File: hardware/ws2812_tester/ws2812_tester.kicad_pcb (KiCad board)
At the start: 2 copper layers, 25 x 25 mm, 14 parts, among them J1 USB_C_DEALON-USB-US31-106, J2 Pins_1-4, J3 Conn_01x03, J4 Pins_5-8, U1 ATtiny85-20S

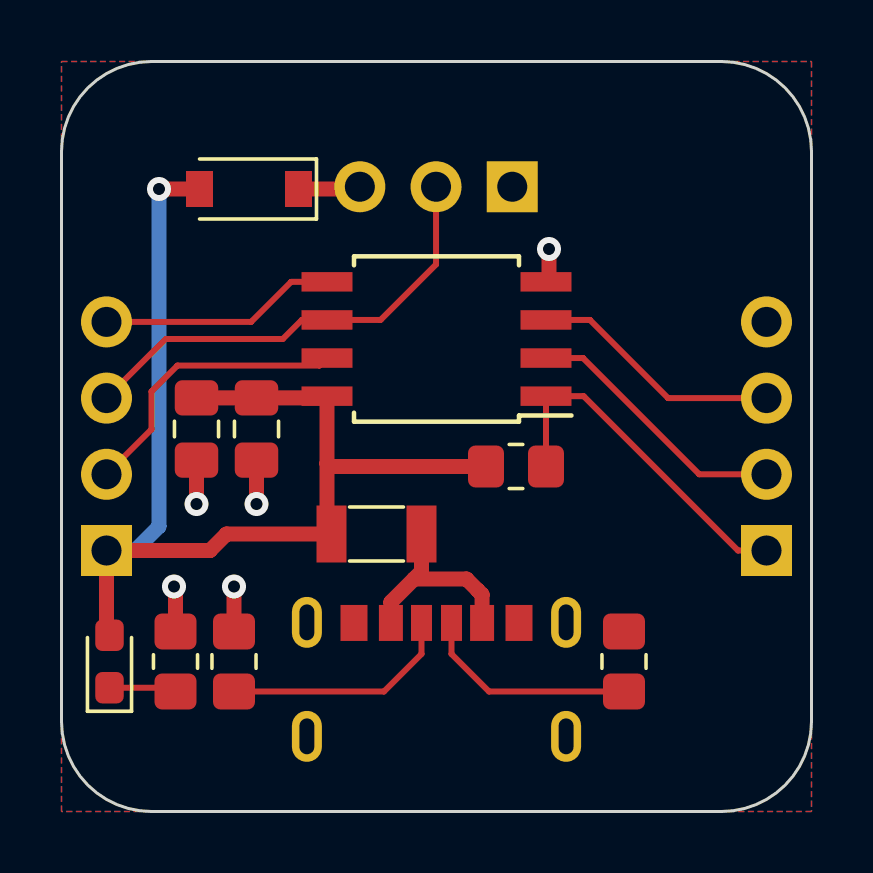
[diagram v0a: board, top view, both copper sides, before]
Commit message: Moves LED connector closer to the edge
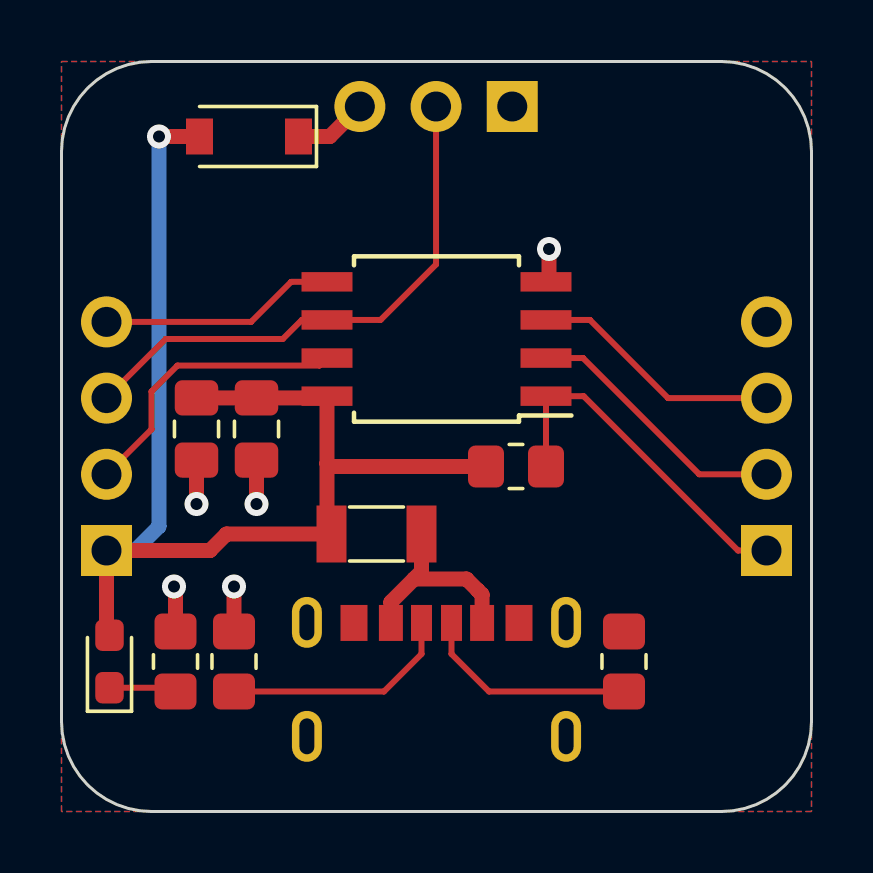
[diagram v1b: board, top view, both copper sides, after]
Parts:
- moved J3 2.67 mm to (153.0, 101.5)
- moved D2 1.75 mm to (144.2, 102.5)
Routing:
- net PB1/LED_DATA: track 15.4 -> 18.1 mm
- net VCC: track 39.6 -> 41.4 mm
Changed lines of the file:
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@@
   )
   (footprint "Diode_SMD:D_SOD-123" (layer "F.Cu")
-    (at 144.25 104.25 180)
+    (at 144.25 102.5 180)
     (descr "SOD-123")
     (tags "SOD-123")
@@
   )
   (footprint "Connector_PinHeader_2.54mm:PinHeader_1x03_P2.54mm_Horizontal" (layer "B.Cu")
-    (at 153.025 104.175 90)
+    (at 153.025 101.5 90)
     (descr "Through hole angled pin header, 1x03, 2.54mm pitch, 6mm pin length, single row")
     (tags "Through hole angled pin header THT 1x03 2.54mm single row")
@@
   (segment (start 152.15 113.5) (end 146.95 113.5) (width 0.5) (layer "F.Cu") (net 1))
   (segment (start 139.5 116.3) (end 142.95 116.3) (width 0.5) (layer "F.Cu") (net 1))
-  (segment (start 141.25 104.25) (end 142.6 104.25) (width 0.5) (layer "F.Cu") (net 1))
   (segment (start 146.85 111.155) (end 146.85 113.4) (width 0.5) (layer "F.Cu") (net 1))
   (segment (start 146.85 113.4) (end 146.85 115.6) (width 0.5) (layer "F.Cu") (net 1))
   (segment (start 142.95 116.3) (end 143.5 115.75) (width 0.5) (layer "F.Cu") (net 1))
+  (segment (start 141.25 102.5) (end 142.6 102.5) (width 0.5) (layer "F.Cu") (net 1))
   (segment (start 139.5 119.025) (end 139.6 119.125) (width 0.5) (layer "F.Cu") (net 1))
   (segment (start 146.95 113.5) (end 146.85 113.4) (width 0.5) (layer "F.Cu") (net 1))
@@
   (segment (start 143.5 115.75) (end 147 115.75) (width 0.5) (layer "F.Cu") (net 1))
   (segment (start 139.5 116.3) (end 139.5 119.025) (width 0.5) (layer "F.Cu") (net 1))
-  (via (at 141.25 104.25) (size 0.8) (drill 0.4) (layers "F.Cu" "B.Cu") (net 1))
-  (segment (start 141.25 115.5) (end 141.25 104.25) (width 0.5) (layer "B.Cu") (net 1))
-  (segment (start 139.5 116.3) (end 140.45 116.3) (width 0.5) (layer "B.Cu") (net 1))
-  (segment (start 140.45 116.3) (end 141.25 115.5) (width 0.5) (layer "B.Cu") (net 1))
+  (via (at 141.25 102.5) (size 0.8) (drill 0.4) (layers "F.Cu" "B.Cu") (net 1))
+  (segment (start 141.25 115.5) (end 140.45 116.3) (width 0.5) (layer "B.Cu") (net 1))
+  (segment (start 141.25 102.5) (end 141.25 115.5) (width 0.5) (layer "B.Cu") (net 1))
+  (segment (start 140.45 116.3) (end 139.5 116.3) (width 0.5) (layer "B.Cu") (net 1))
   (segment (start 154.25 106.25) (end 154.25 107.245) (width 0.5) (layer "F.Cu") (net 2))
   (segment (start 154.25 107.245) (end 154.15 107.345) (width 0.5) (layer "F.Cu") (net 2))
@@
   (via (at 143.75 117.5) (size 0.8) (drill 0.4) (layers "F.Cu" "B.Cu") (net 2))
   (via (at 142.5 114.75) (size 0.8) (drill 0.4) (layers "F.Cu" "B.Cu") (net 2))
-  (segment (start 147.87 104.25) (end 147.945 104.175) (width 0.5) (layer "F.Cu") (net 3))
-  (segment (start 145.9 104.25) (end 147.87 104.25) (width 0.5) (layer "F.Cu") (net 3))
+  (segment (start 145.9 102.5) (end 146.945 102.5) (width 0.5) (layer "F.Cu") (net 3))
+  (segment (start 146.945 102.5) (end 147.945 101.5) (width 0.5) (layer "F.Cu") (net 3))
   (segment (start 149.75 117.25) (end 151.5 117.25) (width 0.5) (layer "F.Cu") (net 4))
   (segment (start 152.02 117.77) (end 152.02 118.715) (width 0.5) (layer "F.Cu") (net 4))
@@
   (segment (start 158.22 111.22) (end 161.5 111.22) (width 0.2) (layer "F.Cu") (net 9))
   (segment (start 154.15 108.615) (end 155.615 108.615) (width 0.2) (layer "F.Cu") (net 9))
+  (segment (start 150.485 106.765) (end 150.485 101.5) (width 0.2) (layer "F.Cu") (net 10))
   (segment (start 146.01 108.615) (end 146.85 108.615) (width 0.2) (layer "F.Cu") (net 10))
   (segment (start 146.85 108.615) (end 148.635 108.615) (width 0.2) (layer "F.Cu") (net 10))
-  (segment (start 150.485 106.765) (end 150.485 104.175) (width 0.2) (layer "F.Cu") (net 10))
   (segment (start 141.47 109.25) (end 145.375 109.25) (width 0.2) (layer "F.Cu") (net 10))
   (segment (start 145.375 109.25) (end 146.01 108.615) (width 0.2) (layer "F.Cu") (net 10))
+  (segment (start 139.5 111.22) (end 141.47 109.25) (width 0.2) (layer "F.Cu") (net 10))
   (segment (start 148.635 108.615) (end 150.485 106.765) (width 0.2) (layer "F.Cu") (net 10))
-  (segment (start 139.5 111.22) (end 141.47 109.25) (width 0.2) (layer "F.Cu") (net 10))
   (segment (start 141 111) (end 141 112.26) (width 0.2) (layer "F.Cu") (net 11))
   (segment (start 141 112.26) (end 139.5 113.76) (width 0.2) (layer "F.Cu") (net 11))

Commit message: Adds labels for the Pins
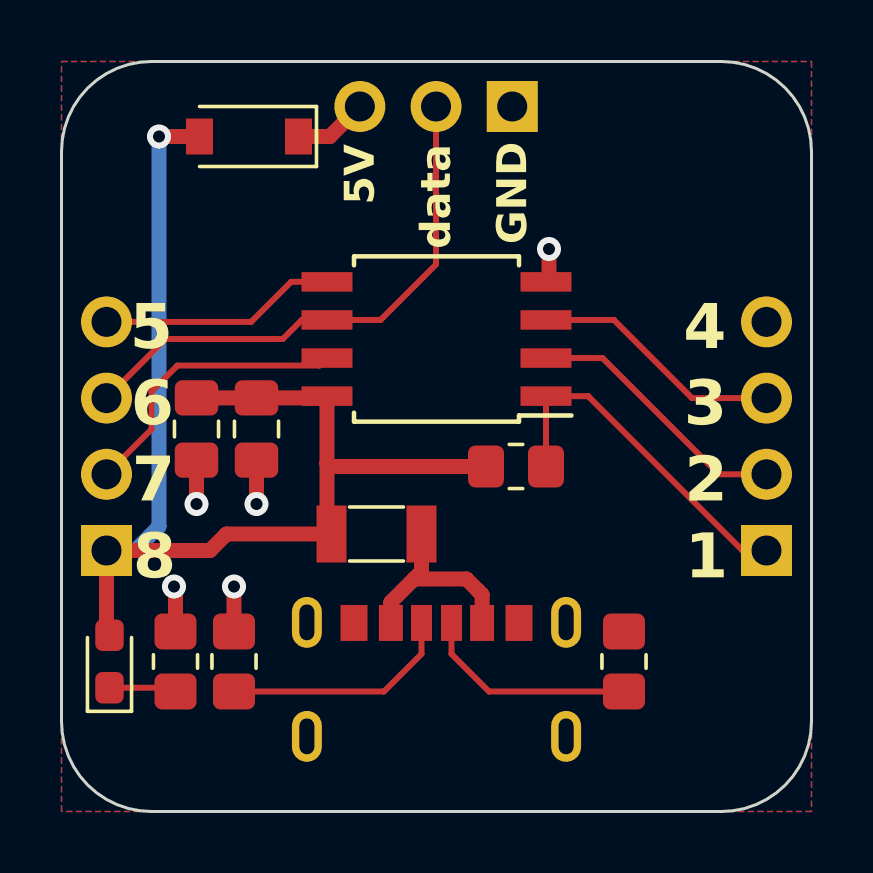
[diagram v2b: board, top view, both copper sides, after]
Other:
- board text added: "1"
- board text added: "2"
- board text added: "3"
- board text added: "4"
- board text added: "5"
- board text added: "5V"
- board text added: "6"
- board text added: "7"
- board text added: "8"
- board text added: "GND"
- board text added: "data"
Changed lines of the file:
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@@
   (gr_arc (start 138 103) (mid 138.87868 100.87868) (end 141 100)
     (stroke (width 0.1) (type default)) (layer "Edge.Cuts"))
+  (gr_text "6" (at 141.029377 111.397264) (layer "F.SilkS")
+    (effects (font (size 1.5 1.5) (thickness 0.3) bold))
+  )
+  (gr_text "data" (at 150.485 104.5 90) (layer "F.SilkS")
+    (effects (font (size 1 1) (thickness 0.25) bold))
+  )
+  (gr_text "4" (at 159.444363 108.854861) (layer "F.SilkS")
+    (effects (font (size 1.5 1.5) (thickness 0.3) bold))
+  )
+  (gr_text "2" (at 159.485232 113.939667) (layer "F.SilkS")
+    (effects (font (size 1.5 1.5) (thickness 0.3) bold))
+  )
+  (gr_text "GND" (at 153.025 104.380952 90) (layer "F.SilkS")
+    (effects (font (size 1 1) (thickness 0.25) bold))
+  )
+  (gr_text "8" (at 141.1 116.5) (layer "F.SilkS")
+    (effects (font (size 1.5 1.5) (thickness 0.3) bold))
+  )
+  (gr_text "1" (at 159.5 116.5) (layer "F.SilkS")
+    (effects (font (size 1.5 1.5) (thickness 0.3) bold))
+  )
+  (gr_text "5" (at 140.994066 108.854861) (layer "F.SilkS")
+    (effects (font (size 1.5 1.5) (thickness 0.3) bold))
+  )
+  (gr_text "5V" (at 147.945 103.761904 90) (layer "F.SilkS")
+    (effects (font (size 1 1) (thickness 0.25) bold))
+  )
+  (gr_text "3" (at 159.464797 111.397264) (layer "F.SilkS")
+    (effects (font (size 1.5 1.5) (thickness 0.3) bold))
+  )
+  (gr_text "7" (at 141.064688 113.939667) (layer "F.SilkS")
+    (effects (font (size 1.5 1.5) (thickness 0.3) bold))
+  )
   (segment (start 152.15 113.5) (end 146.95 113.5) (width 0.5) (layer "F.Cu") (net 1))
   (segment (start 139.5 116.3) (end 142.95 116.3) (width 0.5) (layer "F.Cu") (net 1))
@@
   (segment (start 151 118.715) (end 151 119.75) (width 0.2) (layer "F.Cu") (net 6))
   (segment (start 154.15 113.5) (end 154.15 111.155) (width 0.2) (layer "F.Cu") (net 7))
-  (segment (start 155.405 111.155) (end 160.55 116.3) (width 0.2) (layer "F.Cu") (net 7))
-  (segment (start 160.55 116.3) (end 161.5 116.3) (width 0.2) (layer "F.Cu") (net 7))
-  (segment (start 154.15 111.155) (end 155.405 111.155) (width 0.2) (layer "F.Cu") (net 7))
-  (segment (start 155.385 109.885) (end 159.26 113.76) (width 0.2) (layer "F.Cu") (net 8))
-  (segment (start 154.15 109.885) (end 155.385 109.885) (width 0.2) (layer "F.Cu") (net 8))
-  (segment (start 159.26 113.76) (end 161.5 113.76) (width 0.2) (layer "F.Cu") (net 8))
-  (segment (start 155.615 108.615) (end 158.22 111.22) (width 0.2) (layer "F.Cu") (net 9))
-  (segment (start 158.22 111.22) (end 161.5 111.22) (width 0.2) (layer "F.Cu") (net 9))
-  (segment (start 154.15 108.615) (end 155.615 108.615) (width 0.2) (layer "F.Cu") (net 9))
+  (segment (start 155.555 111.155) (end 160.7 116.3) (width 0.2) (layer "F.Cu") (net 7))
+  (segment (start 160.7 116.3) (end 161.5 116.3) (width 0.2) (layer "F.Cu") (net 7))
+  (segment (start 154.15 111.155) (end 155.555 111.155) (width 0.2) (layer "F.Cu") (net 7))
+  (segment (start 154.15 109.885) (end 156.035 109.885) (width 0.2) (layer "F.Cu") (net 8))
+  (segment (start 156.035 109.885) (end 159.91 113.76) (width 0.2) (layer "F.Cu") (net 8))
+  (segment (start 159.91 113.76) (end 161.5 113.76) (width 0.2) (layer "F.Cu") (net 8))
+  (segment (start 156.415 108.615) (end 159.02 111.22) (width 0.2) (layer "F.Cu") (net 9))
+  (segment (start 154.15 108.615) (end 156.415 108.615) (width 0.2) (layer "F.Cu") (net 9))
+  (segment (start 159.02 111.22) (end 161.5 111.22) (width 0.2) (layer "F.Cu") (net 9))
   (segment (start 150.485 106.765) (end 150.485 101.5) (width 0.2) (layer "F.Cu") (net 10))
   (segment (start 146.01 108.615) (end 146.85 108.615) (width 0.2) (layer "F.Cu") (net 10))

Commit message: Adds logo
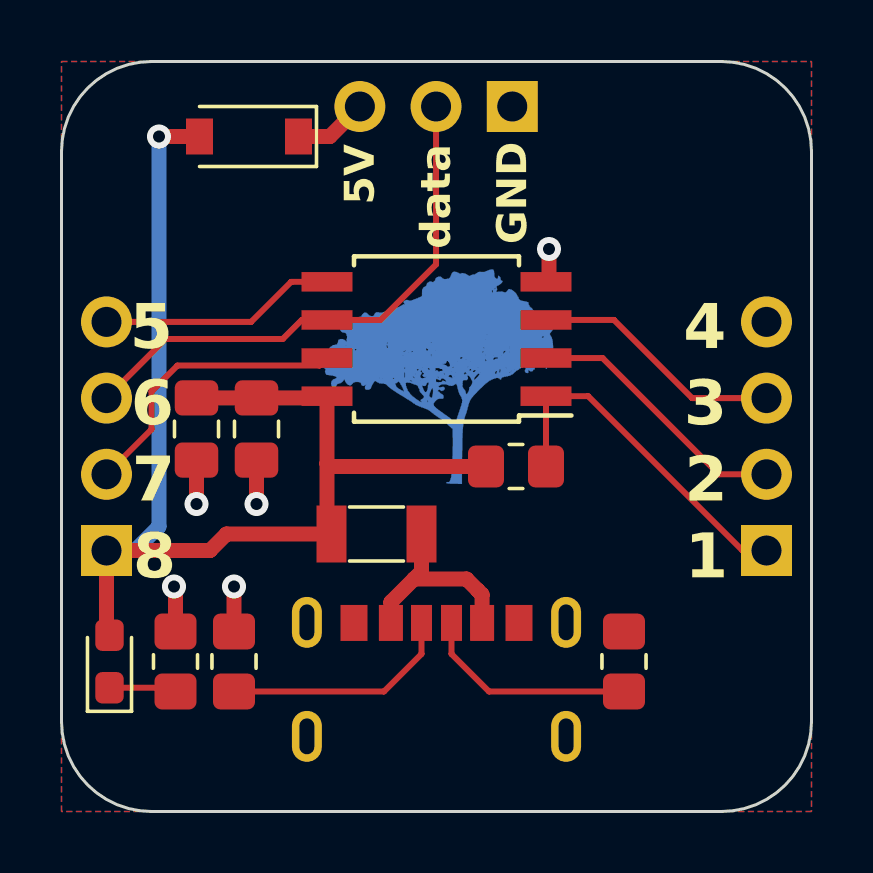
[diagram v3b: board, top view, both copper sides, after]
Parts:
- added Ref**: Val**, Amieiro:url_bsilks, F.Cu at (150.5, 116.0)
- added Ref**: Val**, Amieiro:ipe_logo, F.Cu at (150.5, 110.5)

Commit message: Adds a couple of stitching vias on the top of the PCB
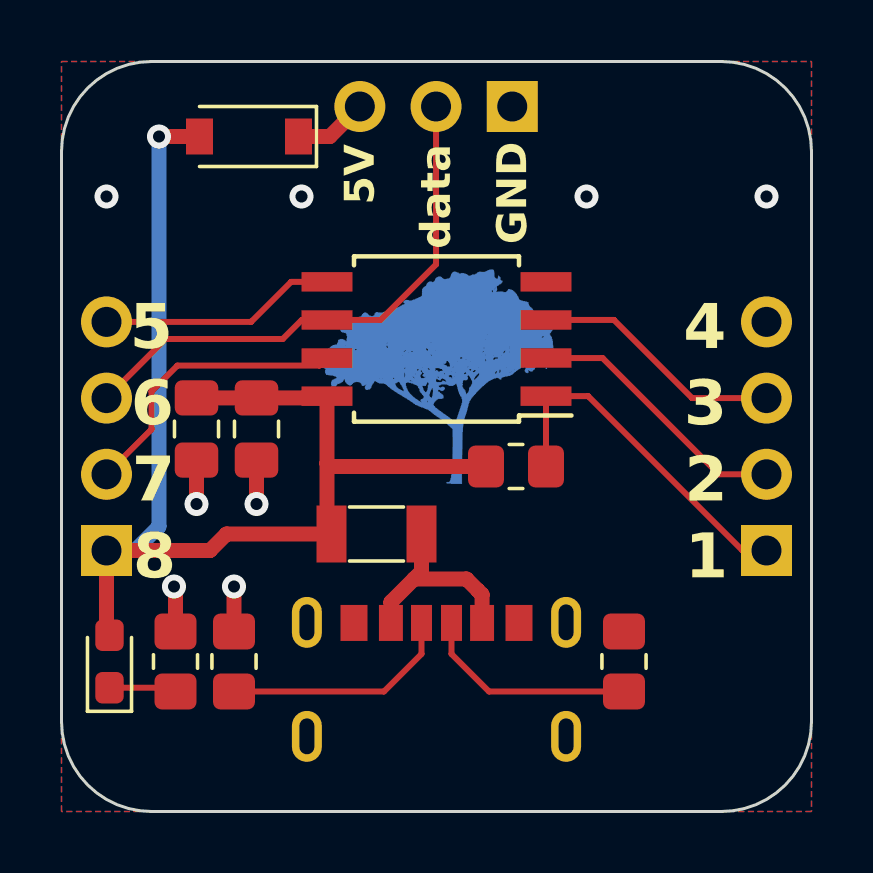
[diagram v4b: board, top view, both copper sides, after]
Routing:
- net GND: track 7.08 -> 5.95 mm, vias 5 -> 8
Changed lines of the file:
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@@
   (segment (start 141.25 102.5) (end 141.25 115.5) (width 0.5) (layer "B.Cu") (net 1))
   (segment (start 140.45 116.3) (end 139.5 116.3) (width 0.5) (layer "B.Cu") (net 1))
-  (segment (start 154.25 106.25) (end 154.25 107.245) (width 0.5) (layer "F.Cu") (net 2))
-  (segment (start 154.25 107.245) (end 154.15 107.345) (width 0.5) (layer "F.Cu") (net 2))
   (segment (start 142.5 113.2875) (end 142.5 114.75) (width 0.5) (layer "F.Cu") (net 2))
   (segment (start 143.75 119) (end 143.75 117.5) (width 0.5) (layer "F.Cu") (net 2))
@@
   (segment (start 141.8 119) (end 141.8 117.55) (width 0.5) (layer "F.Cu") (net 2))
   (via (at 144.5 114.75) (size 0.8) (drill 0.4) (layers "F.Cu" "B.Cu") (net 2))
+  (via (at 146 104.5) (size 0.8) (drill 0.4) (layers "F.Cu" "B.Cu") (free) (net 2))
+  (via (at 161.5 104.5) (size 0.8) (drill 0.4) (layers "F.Cu" "B.Cu") (free) (net 2))
+  (via (at 139.5 104.5) (size 0.8) (drill 0.4) (layers "F.Cu" "B.Cu") (free) (net 2))
   (via (at 141.75 117.5) (size 0.8) (drill 0.4) (layers "F.Cu" "B.Cu") (net 2))
-  (via (at 154.25 106.25) (size 0.8) (drill 0.4) (layers "F.Cu" "B.Cu") (net 2))
+  (via (at 155.5 104.5) (size 0.8) (drill 0.4) (layers "F.Cu" "B.Cu") (free) (net 2))
   (via (at 143.75 117.5) (size 0.8) (drill 0.4) (layers "F.Cu" "B.Cu") (net 2))
   (via (at 142.5 114.75) (size 0.8) (drill 0.4) (layers "F.Cu" "B.Cu") (net 2))

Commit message: Adds JLCPCB order number placeholder
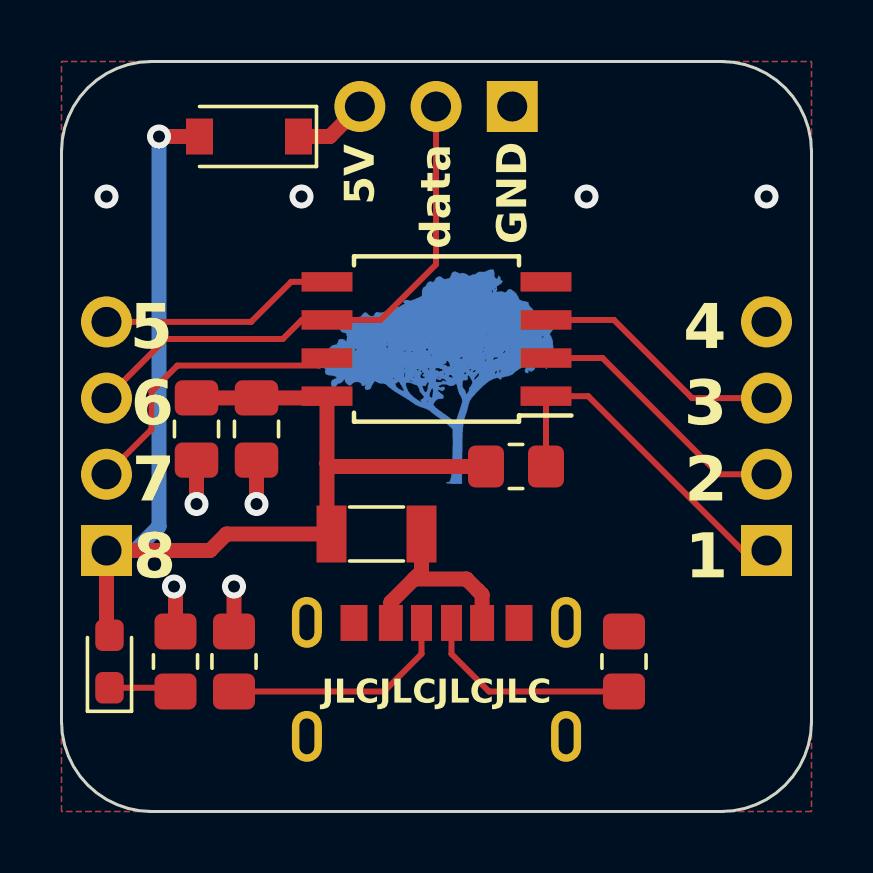
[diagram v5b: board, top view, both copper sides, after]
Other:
- board text added: "JLCJLCJLCJLC"
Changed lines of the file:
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@@
     (effects (font (size 1.5 1.5) (thickness 0.3) bold))
+  )
+  (gr_text "JLCJLCJLCJLC" (at 150.5 121) (layer "F.SilkS")
+    (effects (font (size 0.8 0.8) (thickness 0.2) bold))
   )
   (gr_text "7" (at 141.064688 113.939667) (layer "F.SilkS")

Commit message: Adds revision number to PCB
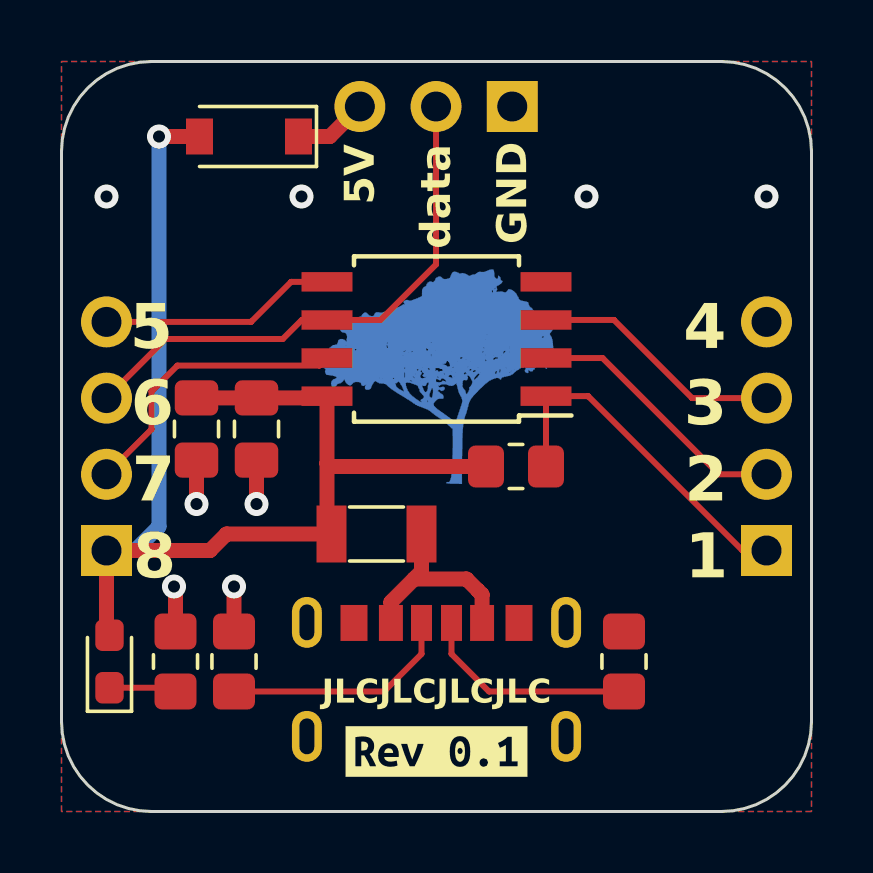
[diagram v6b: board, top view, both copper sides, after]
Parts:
- added kibuzzard-625BD852: G***, kibuzzard-625BD852, F.Cu at (150.5, 123.0)
